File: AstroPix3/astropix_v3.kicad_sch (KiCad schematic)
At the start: 44 parts, among them J1 pcie_GECCO, J10 SPI_right, J2 ChipRings, J3 TempSens, J4 SFOut, J5 sample_clock_out, J6 HV_in_external, J9 SPI_left, U2 SN65LVDS4, U5 AstroPix3_split

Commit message: PCB: Astropix3 updates
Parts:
- added C1: 1nF, Capacitor_SMD:C_0603_1608Metric, symbol Device:C
- added C15: 10uF, Capacitor_SMD:C_0603_1608Metric, symbol Device:C
- added C2: .1uF, Capacitor_SMD:C_0603_1608Metric, symbol Device:C
- added J7: HV_in_ring, Connector_Coaxial:SMA_Molex_73251-2200_Horizontal, symbol Connector:Conn_Coaxial
- added R15, R16, R19, R6, R9: 220k, Resistor_SMD:R_0603_1608Metric, symbol Device:R
- JP1: symbol astropix_v2-rescue:Jumper_3_Bridged12-Jumper -> Jumper:Jumper_3_Bridged12
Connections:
- net GND: now also C1.2, C15.2, C2.2, J7.2 (Ext), R6.1
- net VSSA: now also J1.A5 (VSSA), C1.1, C15.1, C2.1
- net ring1: now also R6.2, R9.1
- net ring2: now also R15.1, R9.2
- net ring3: now also R15.2, R16.1
- net ring4: now also R16.2, R19.1
- new net: J7.1 (In), R19.2
- no-connect marks 59 -> 58
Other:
- moved on the sheet: R2

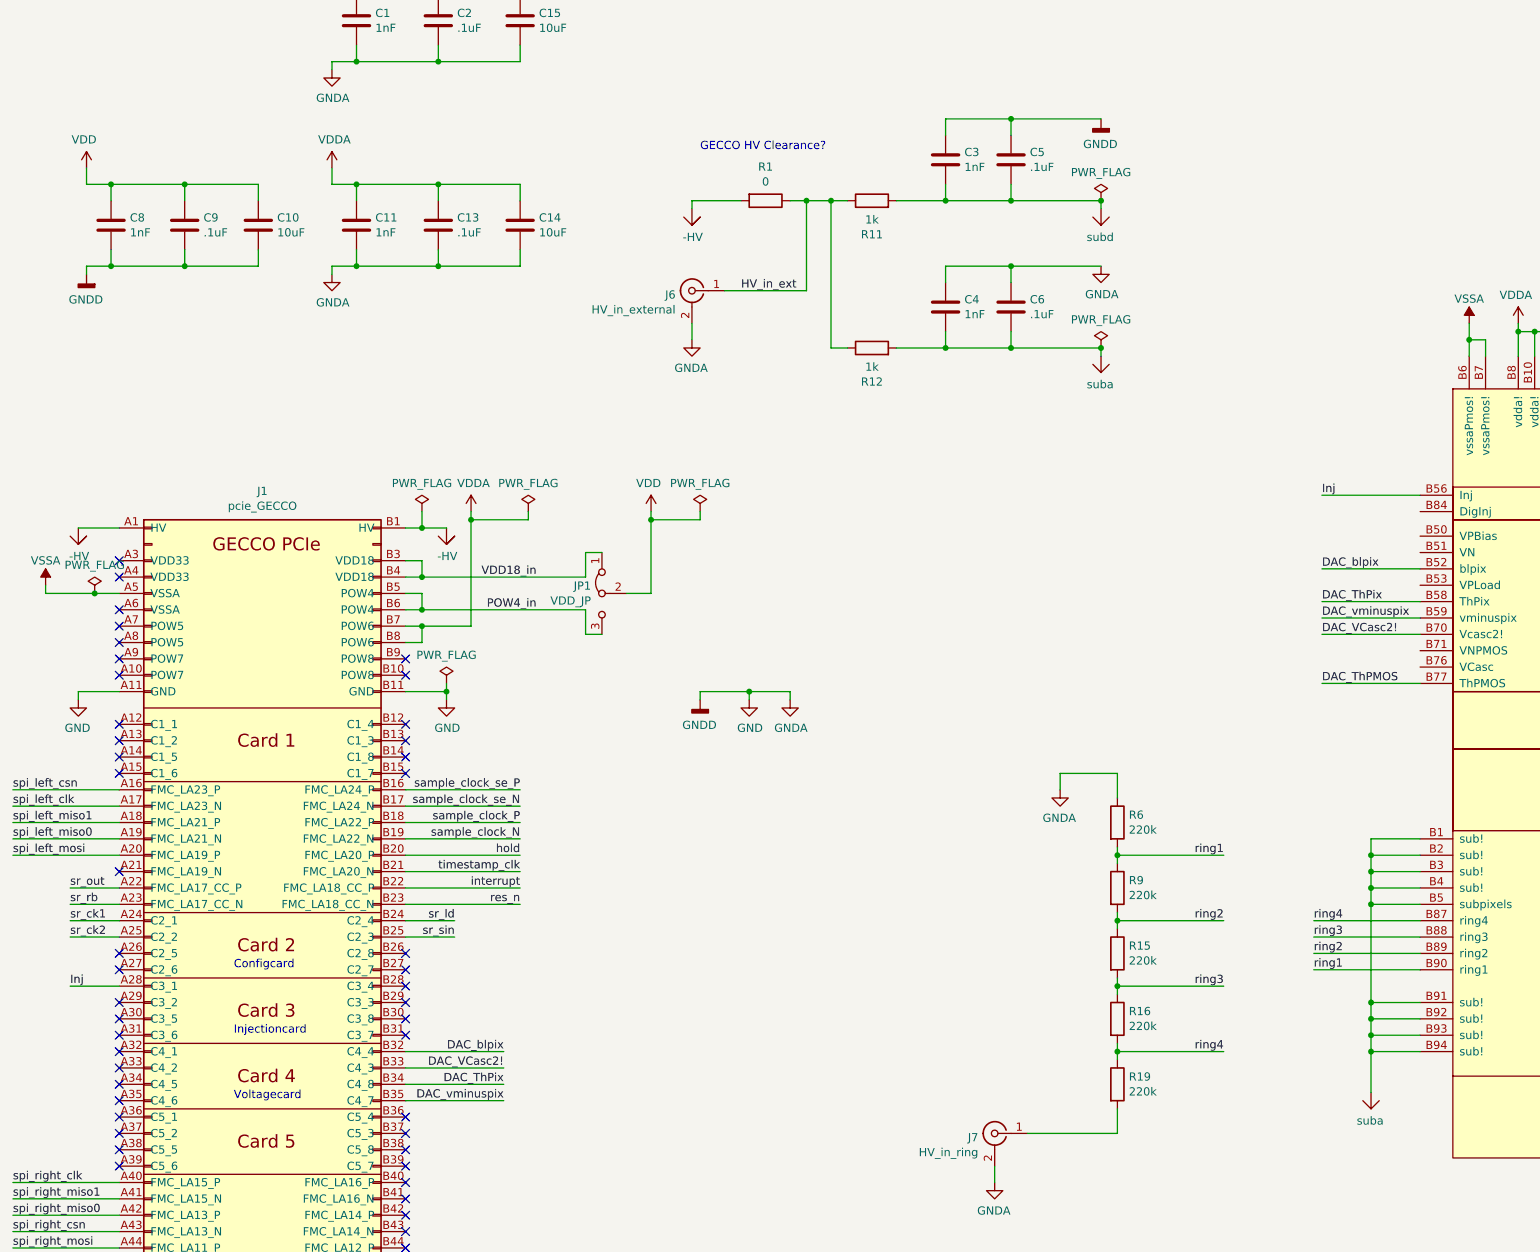
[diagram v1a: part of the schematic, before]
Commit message: PCB: Astropix3 update
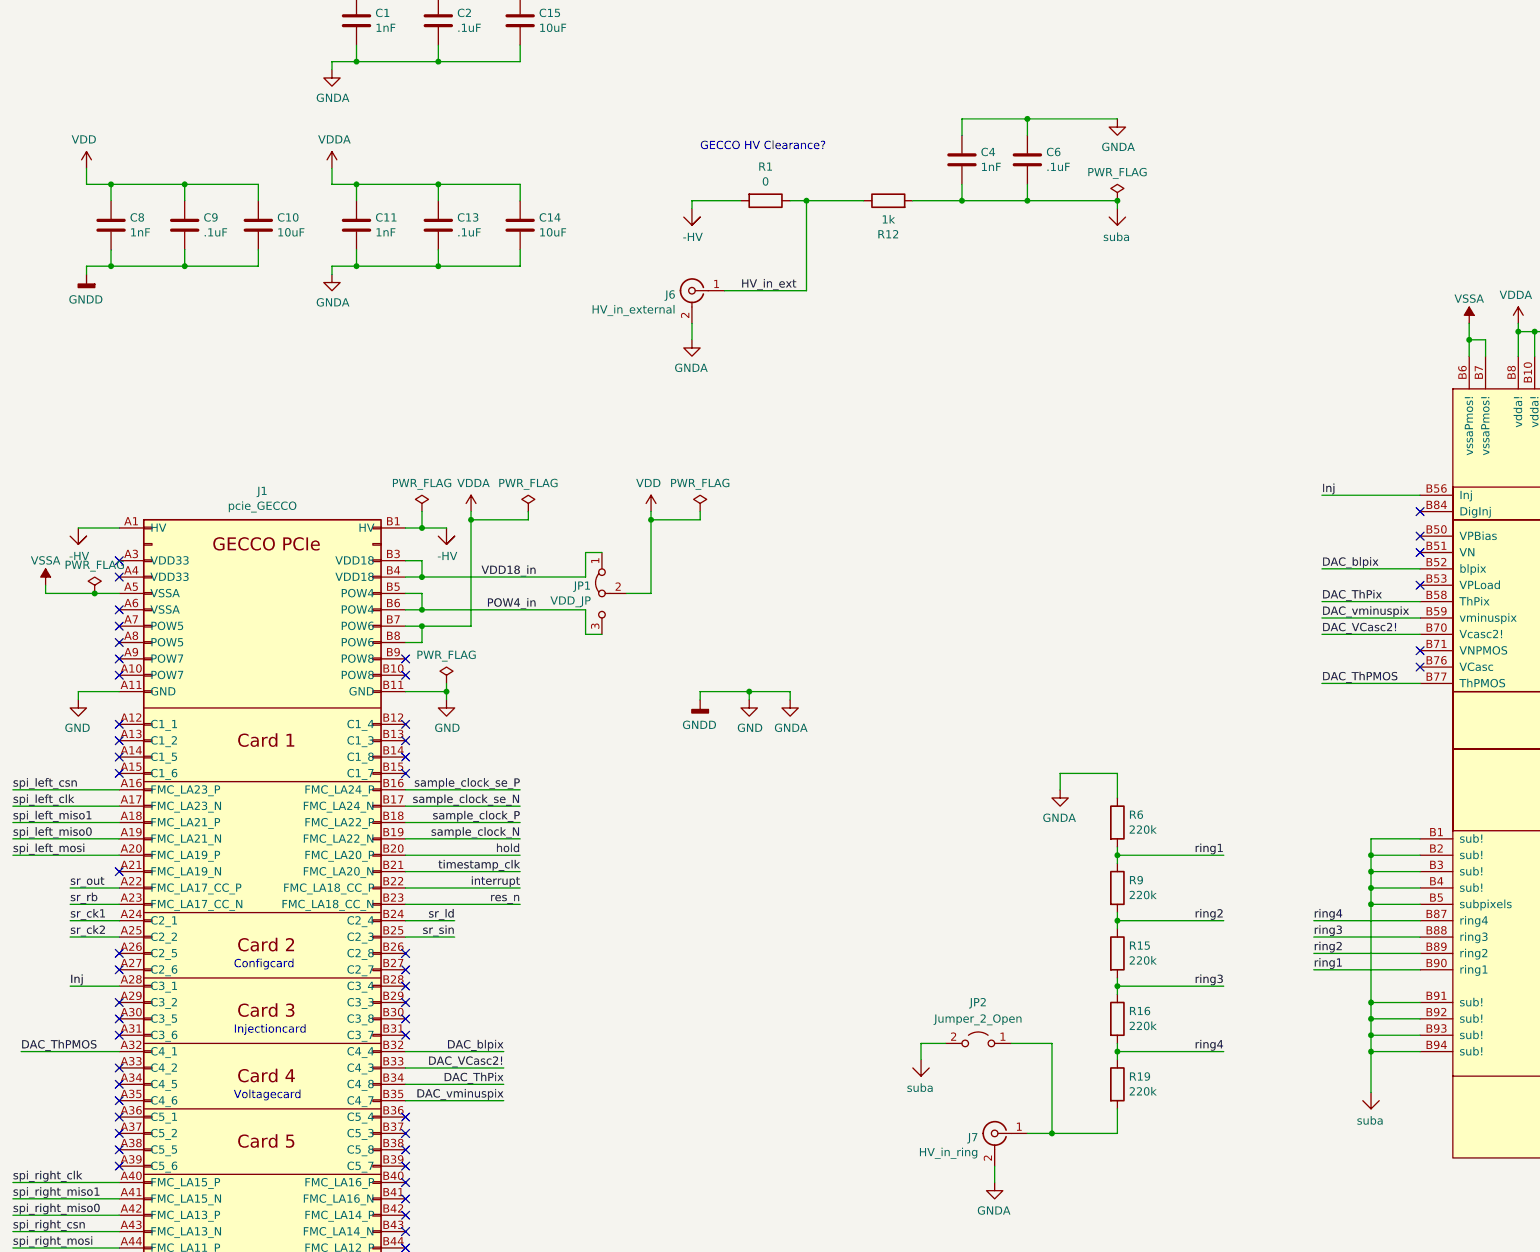
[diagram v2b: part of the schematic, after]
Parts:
- removed C3: 1nF, Capacitor_SMD:C_1210_3225Metric, symbol Device:C
- removed C5: .1uF, Capacitor_SMD:C_1210_3225Metric, symbol Device:C
- removed R11: 1k, Resistor_SMD:R_0603_1608Metric, symbol Device:R
- added JP2: Jumper_2_Open, Connector_PinHeader_2.54mm:PinHeader_1x02_P2.54mm_Vertical, symbol Jumper:Jumper_2_Open
- U2: footprint astropix:Texas_Instruments-SN65LVDS4RSET-0 -> Package_DFN_QFN:Texas_R-PUQFN-N10
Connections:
- net DAC_ThPMOS: now also J1.A32 (C4_1)
- net suba: now also JP2.2 (B)
- net at J7.1 (In), R19.2: now also JP2.1 (A)
- no-connect marks 58 -> 63
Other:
- moved on the sheet: C4, C6, R12

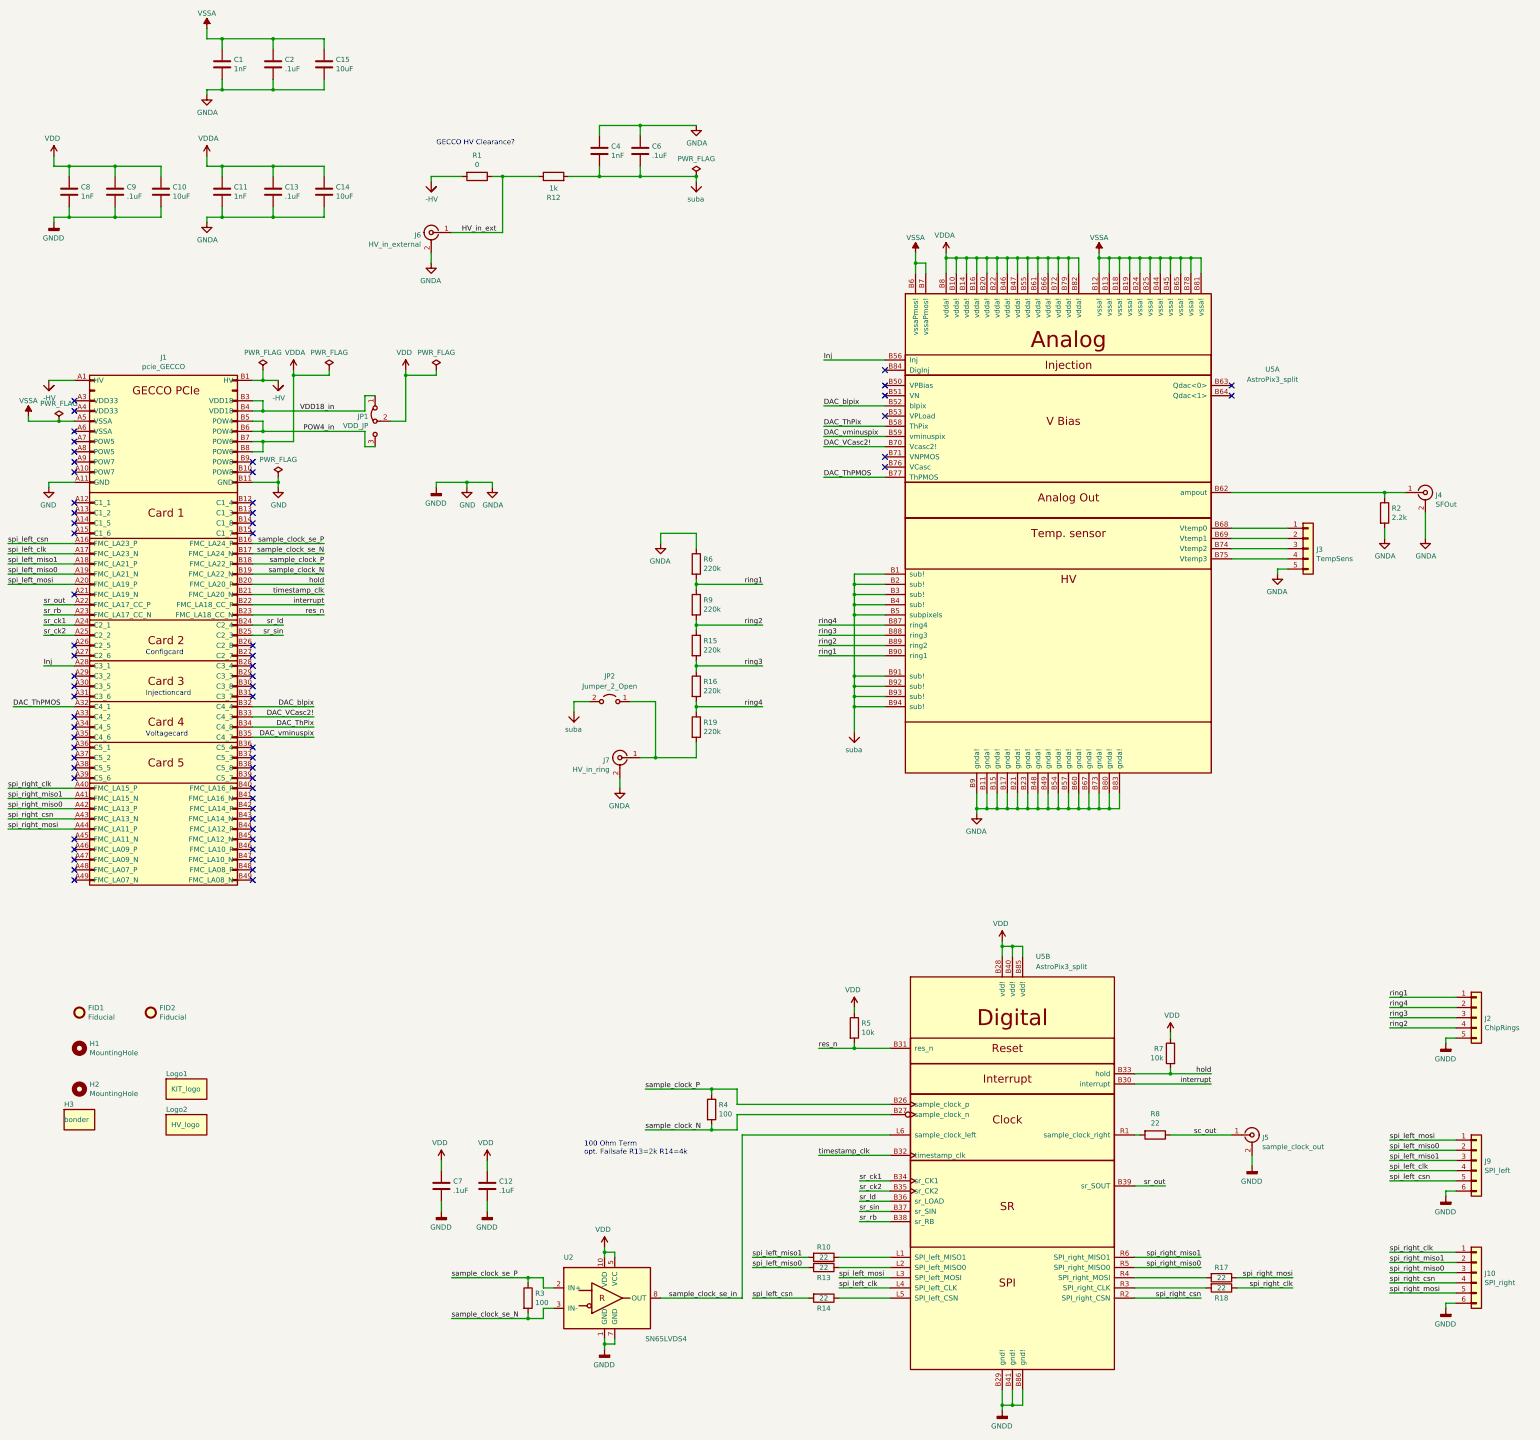
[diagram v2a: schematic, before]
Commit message: PCB: Astropix3 update
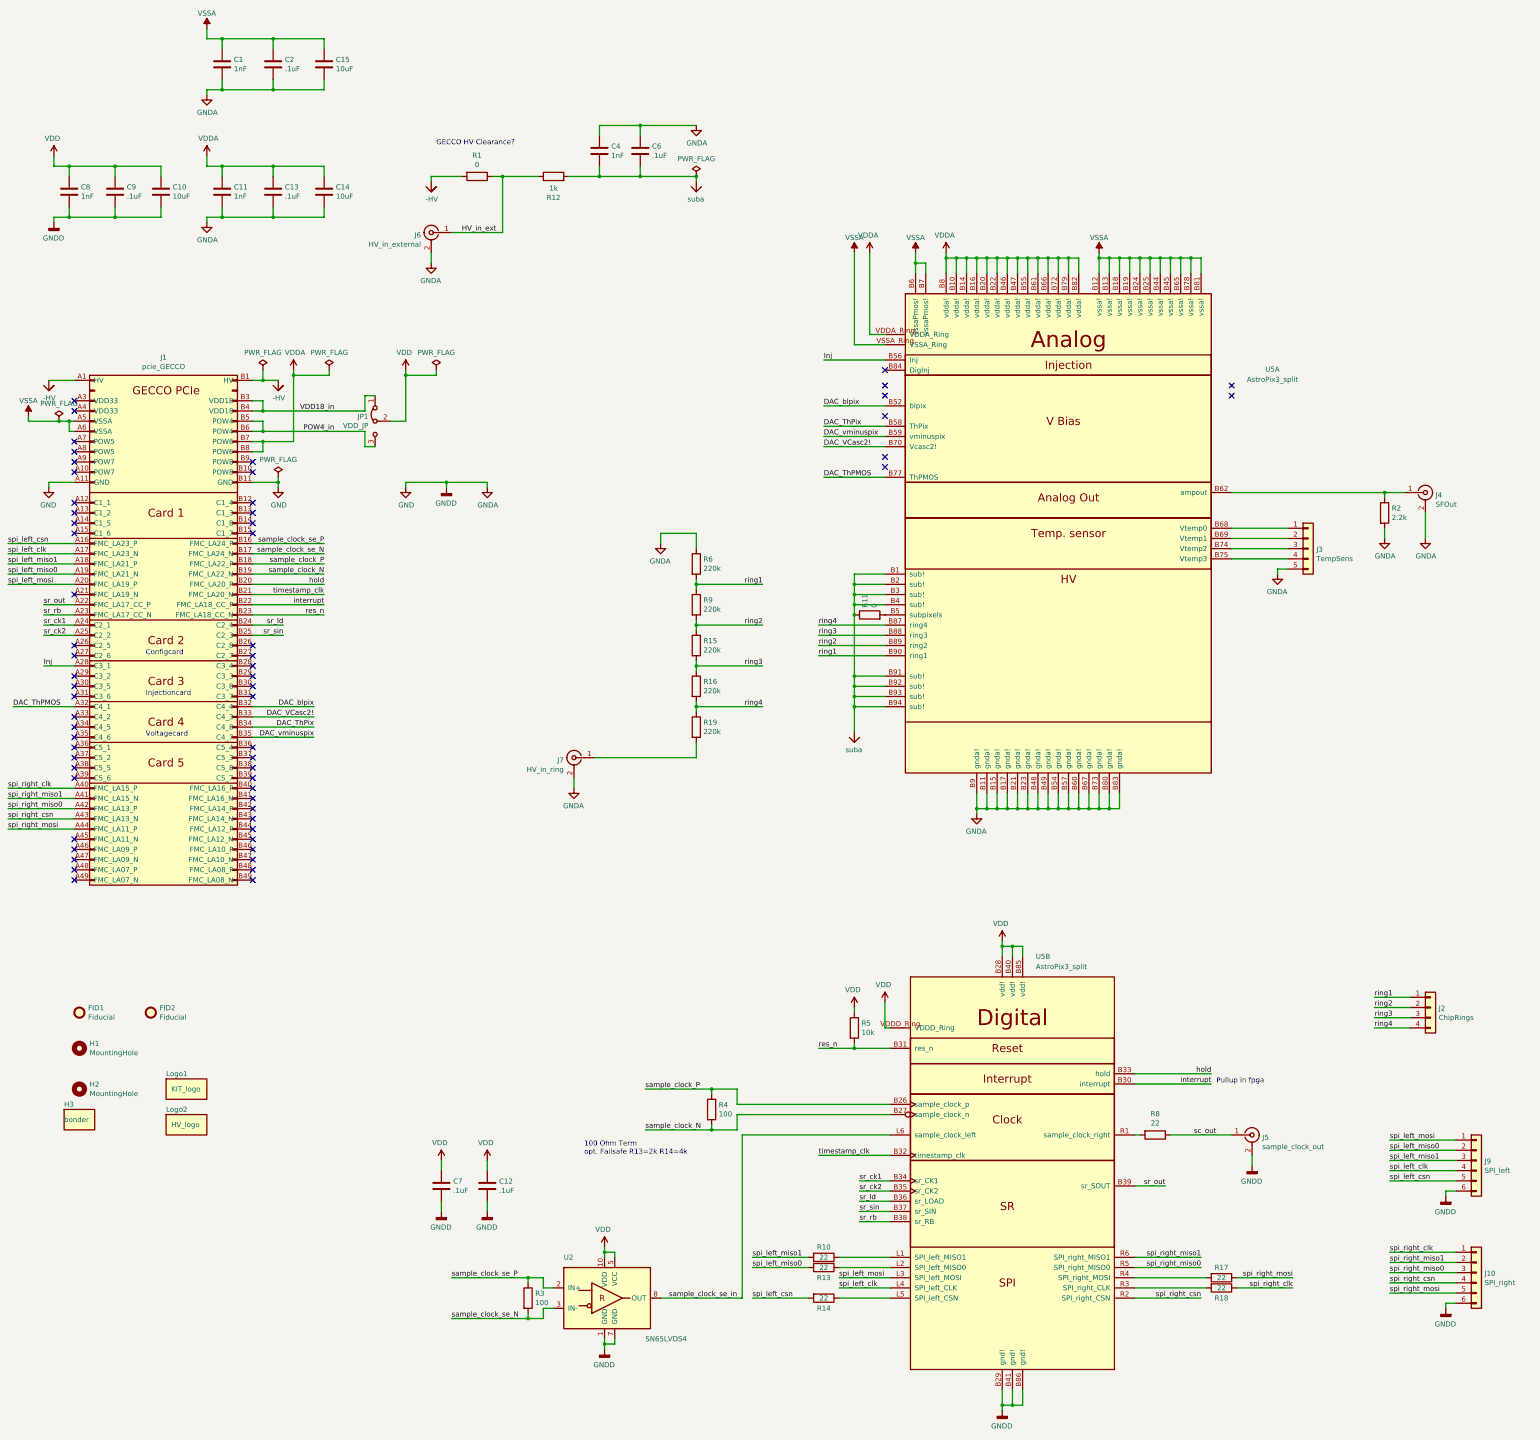
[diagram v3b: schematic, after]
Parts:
- removed J2: ChipRings, Connector_PinHeader_2.54mm:PinHeader_1x05_P2.54mm_Vertical, symbol Connector_Generic:Conn_01x05
- removed JP2: Jumper_2_Open, Connector_PinHeader_2.54mm:PinHeader_1x02_P2.54mm_Vertical, symbol Jumper:Jumper_2_Open
- removed R7: 10k, Resistor_SMD:R_0603_1608Metric, symbol Device:R
- added J2: ChipRings, Connector_PinHeader_2.54mm:PinHeader_1x04_P2.54mm_Vertical, symbol Connector_Generic:Conn_01x04
- added R11: 0, Resistor_SMD:R_0603_1608Metric, symbol Device:R
- U5: footprint astropix:AstroPix3 -> astropix:AstroPix3_power; symbol astropix:AstroPix3_split -> astropix:AstroPix3_split_power
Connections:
- net VDD: now also U5.VDDD_Ring
- net VDDA: now also U5.VDDA_Ring
- net VSSA: now also J1.A6 (VSSA), U5.VSSA_Ring
- net ring1: now also J2.1 (Pin_1)
- net ring2: now also J2.2 (Pin_2)
- net ring3: now also J2.3 (Pin_3)
- net ring4: now also J2.4 (Pin_4)
- net suba: now also R11.1; no longer U5.B5 (subpixels)
- new net: R11.2, U5.B5 (subpixels)
- no-connect marks 63 -> 62
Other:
- note added: "Pullup in fpga"
- moved on the sheet: J7

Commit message: PCB: Added final V3 PCB with fabrication data
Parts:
- removed J7: HV_in_ring, Connector_Coaxial:SMA_Molex_73251-2200_Horizontal, symbol Connector:Conn_Coaxial
- added J7: Conn_01x03, Connector_PinHeader_2.54mm:PinHeader_1x03_P2.54mm_Vertical, symbol Connector_Generic:Conn_01x03
- U5: footprint astropix:AstroPix3_power -> astropix:AstroPix3_power2; symbol astropix:AstroPix3_split_power -> astropix:AstroPix3_split_power2
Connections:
- net GND: now also J7.2 (Pin_2); no longer R6.1
- net VDD: no longer U5.B28 (vdd!), U5.B40 (vdd!), U5.B85 (vdd!)
- net VDDA: no longer U5.B10 (vdda!), U5.B14 (vdda!), U5.B16 (vdda!), U5.B20 (vdda!), U5.B22 (vdda!), U5.B46 (vdda!), U5.B47 (vdda!), U5.B55 (vdda!), U5.B61 (vdda!), U5.B66 (vdda!), U5.B72 (vdda!), U5.B79 (vdda!), U5.B8 (vdda!), U5.B82 (vdda!)
- net VSSA: no longer U5.B12 (vssa!), U5.B13 (vssa!), U5.B18 (vssa!), U5.B19 (vssa!), U5.B24 (vssa!), U5.B25 (vssa!), U5.B44 (vssa!), U5.B45 (vssa!), U5.B6 (vssaPmos!), U5.B65 (vssa!), U5.B7 (vssaPmos!), U5.B78 (vssa!), U5.B81 (vssa!)
- net DigInj: now reaches J1.B40 (FMC_LA16_P)
- net DigInj: now also U5.B84 (DigInj)
- net at R19.2: now also J7.3 (Pin_3)
- new net: J7.1 (Pin_1), R6.1
- no-connect marks 62 -> 53
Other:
- moved on the sheet: J2
